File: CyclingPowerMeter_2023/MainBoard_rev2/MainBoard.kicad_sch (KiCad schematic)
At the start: 21 parts, among them J1 Conn_01x01, J2 Conn_01x01, J3 Conn_01x01, J4 Conn_01x01, J5 Conn_01x01, J6 Conn_01x01, J7 Conn_01x01, J8 Conn_01x01, J9 Conn_01x01, SW1 SW_Push_45deg, U1 AD8236, U2 Seeed_Studio_XIAO_nRF52840_Se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

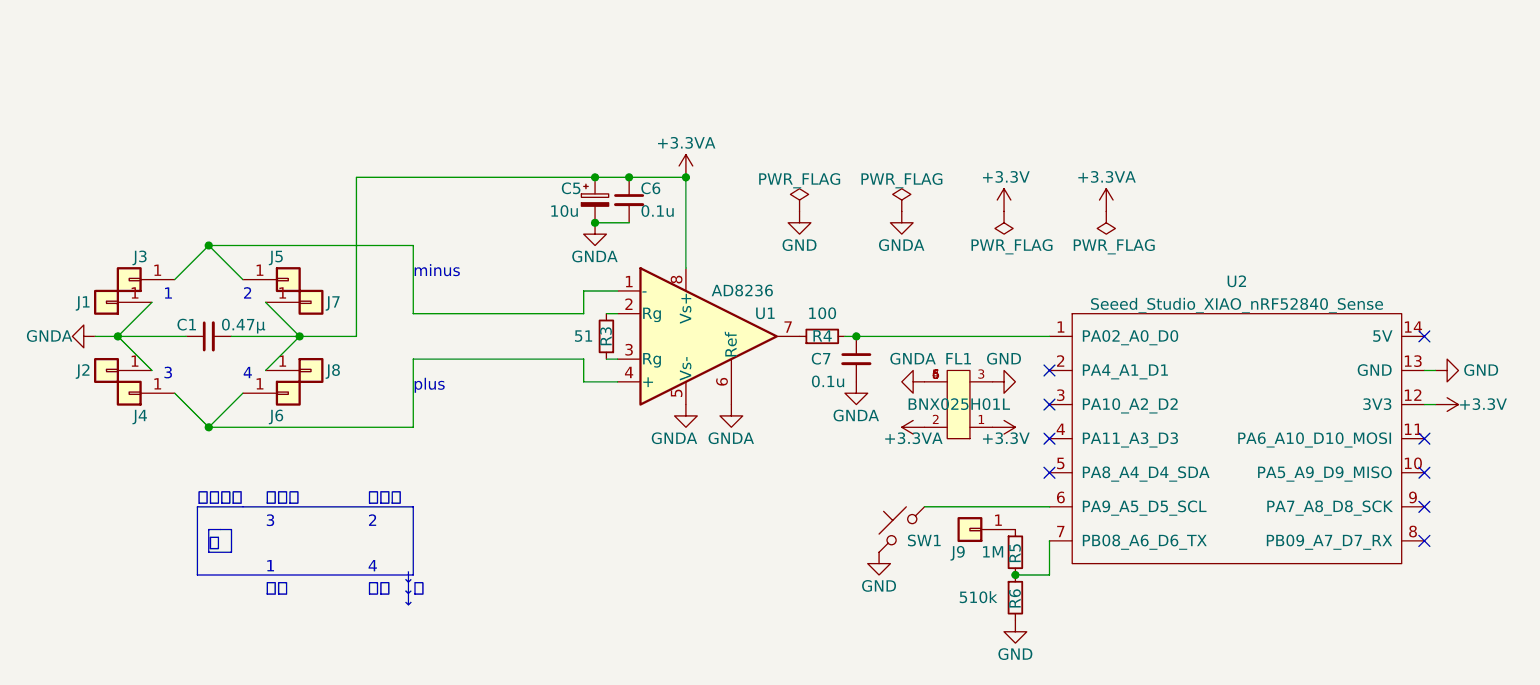
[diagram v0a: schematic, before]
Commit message: パワメのファームを書いた
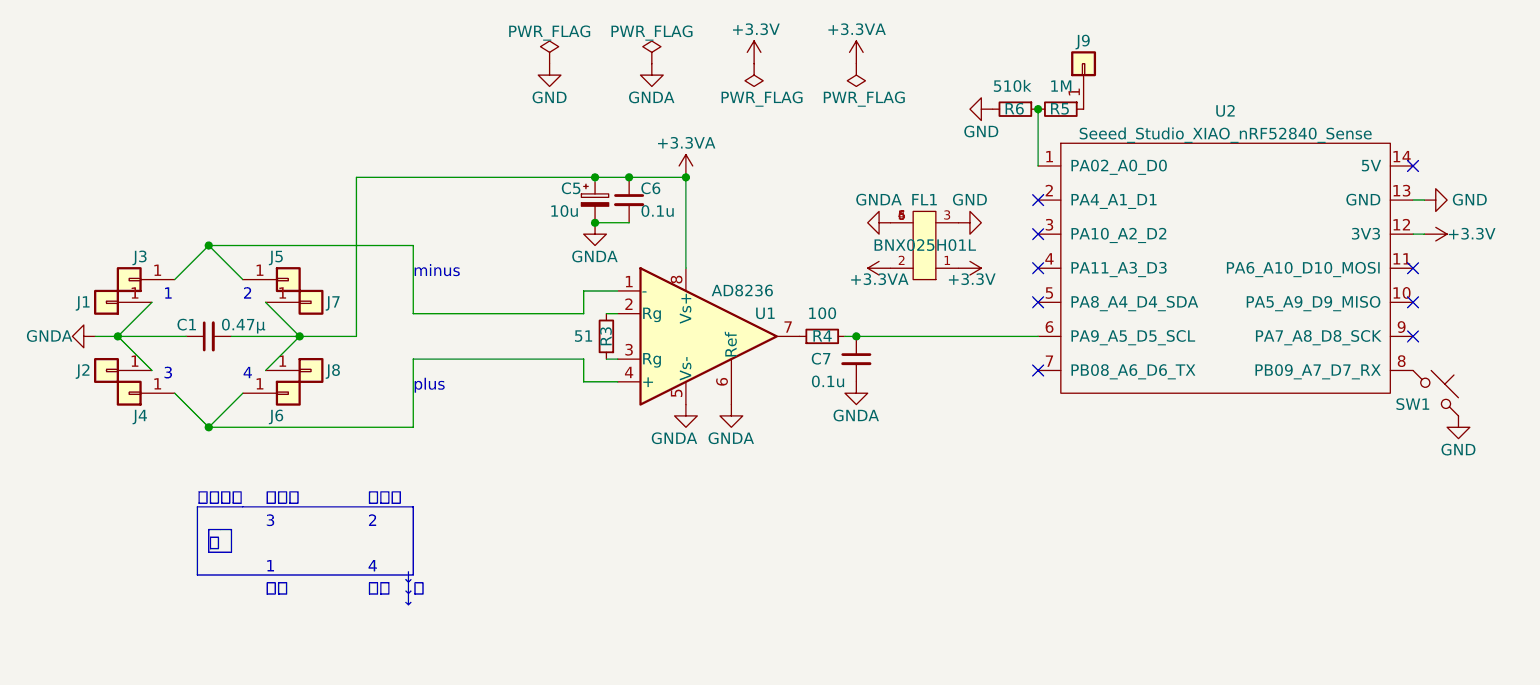
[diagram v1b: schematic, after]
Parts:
- R5, R6: footprint Resistor_SMD:R_0603_1608Metric_Pad0.98x0.95mm_HandSolder -> Resistor_SMD:R_0603_1608Metric
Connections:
- net at C7.1, R4.2: now also U2.6 (PA9_A5_D5_SCL); no longer U2.1 (PA02_A0_D0)
- net at R5.2, R6.1: now also U2.1 (PA02_A0_D0); no longer U2.7 (PB08_A6_D6_TX)
- net at SW1.1: now also U2.8 (PB09_A7_D7_RX); no longer U2.6 (PA9_A5_D5_SCL)
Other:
- moved on the sheet: FL1, J9, R5, R6, SW1, U2
